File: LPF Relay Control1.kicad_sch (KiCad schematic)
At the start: 24 parts, among them K10 EA2-5NU, K3 EA2-5NU, K4 EA2-5NU, K5 EA2-5NU, K6 EA2-5NU, K7 EA2-5NU, K8 EA2-5NU, K9 EA2-5NU, Q1 BSS123, Q3 BSS123, Q4 BSS123, Q6 BSS123

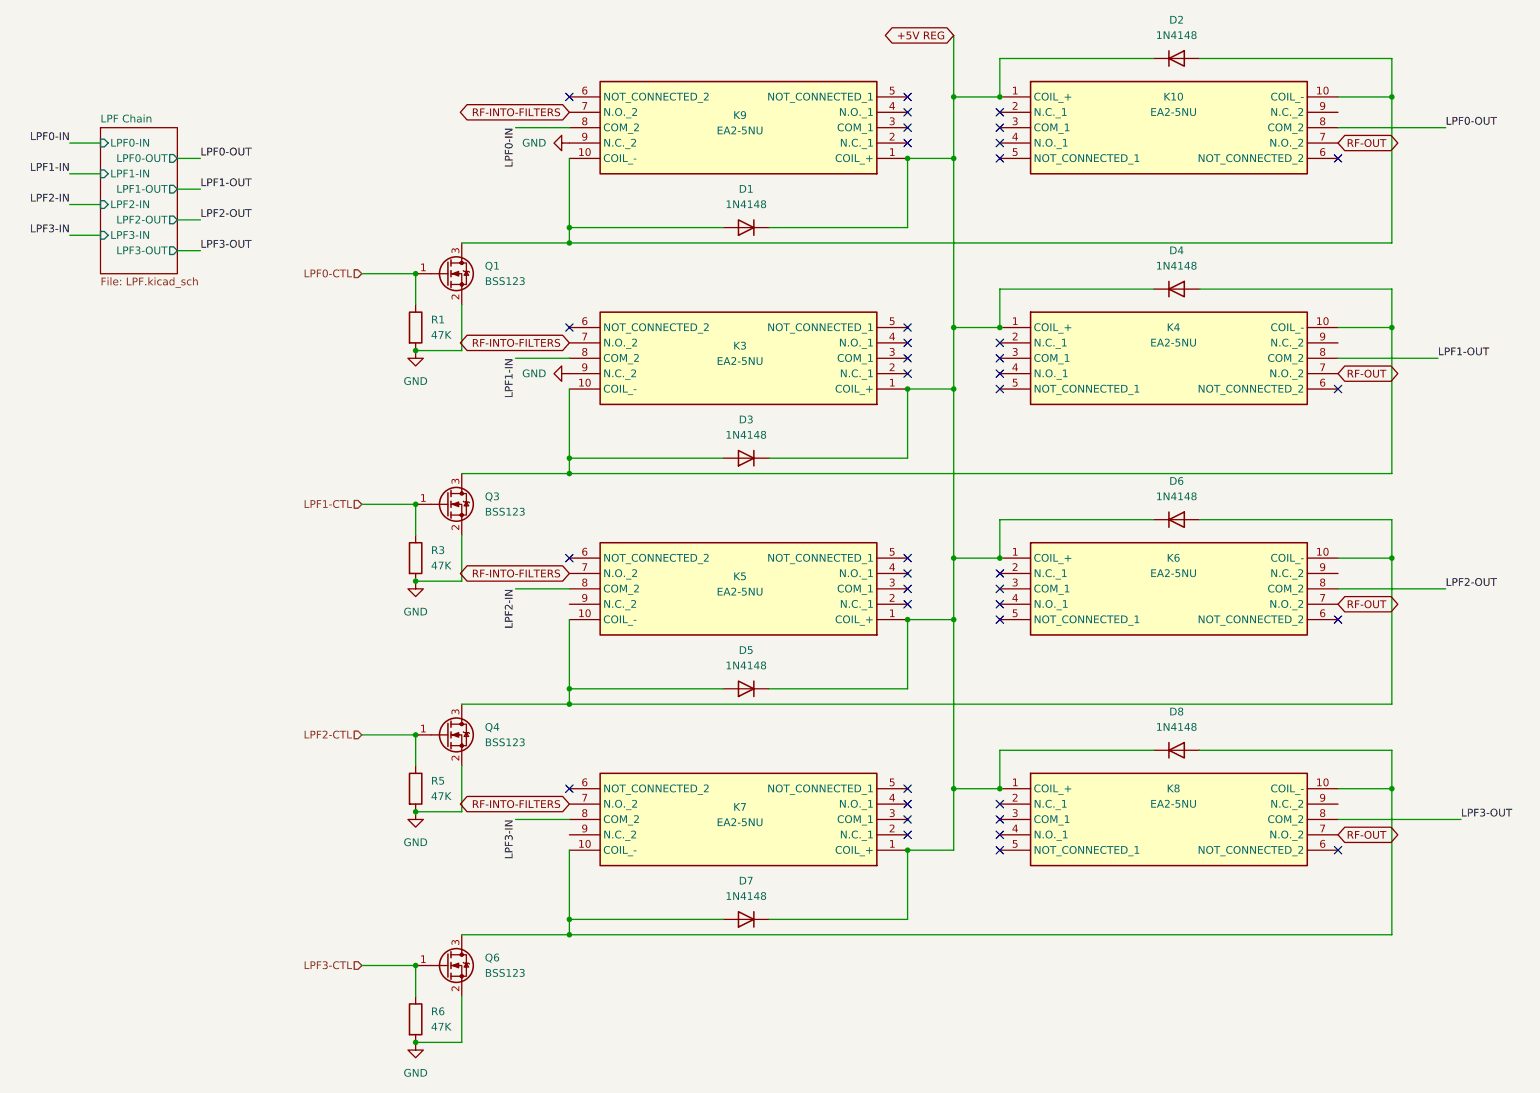
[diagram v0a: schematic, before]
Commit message: v0.6 ERC passes.  I went over it with a fine tooth comb and corrected lots of little stuff.  Ron should review all the components I have to create very carefully.  In particular, MPS-751 symbol does not look correct.
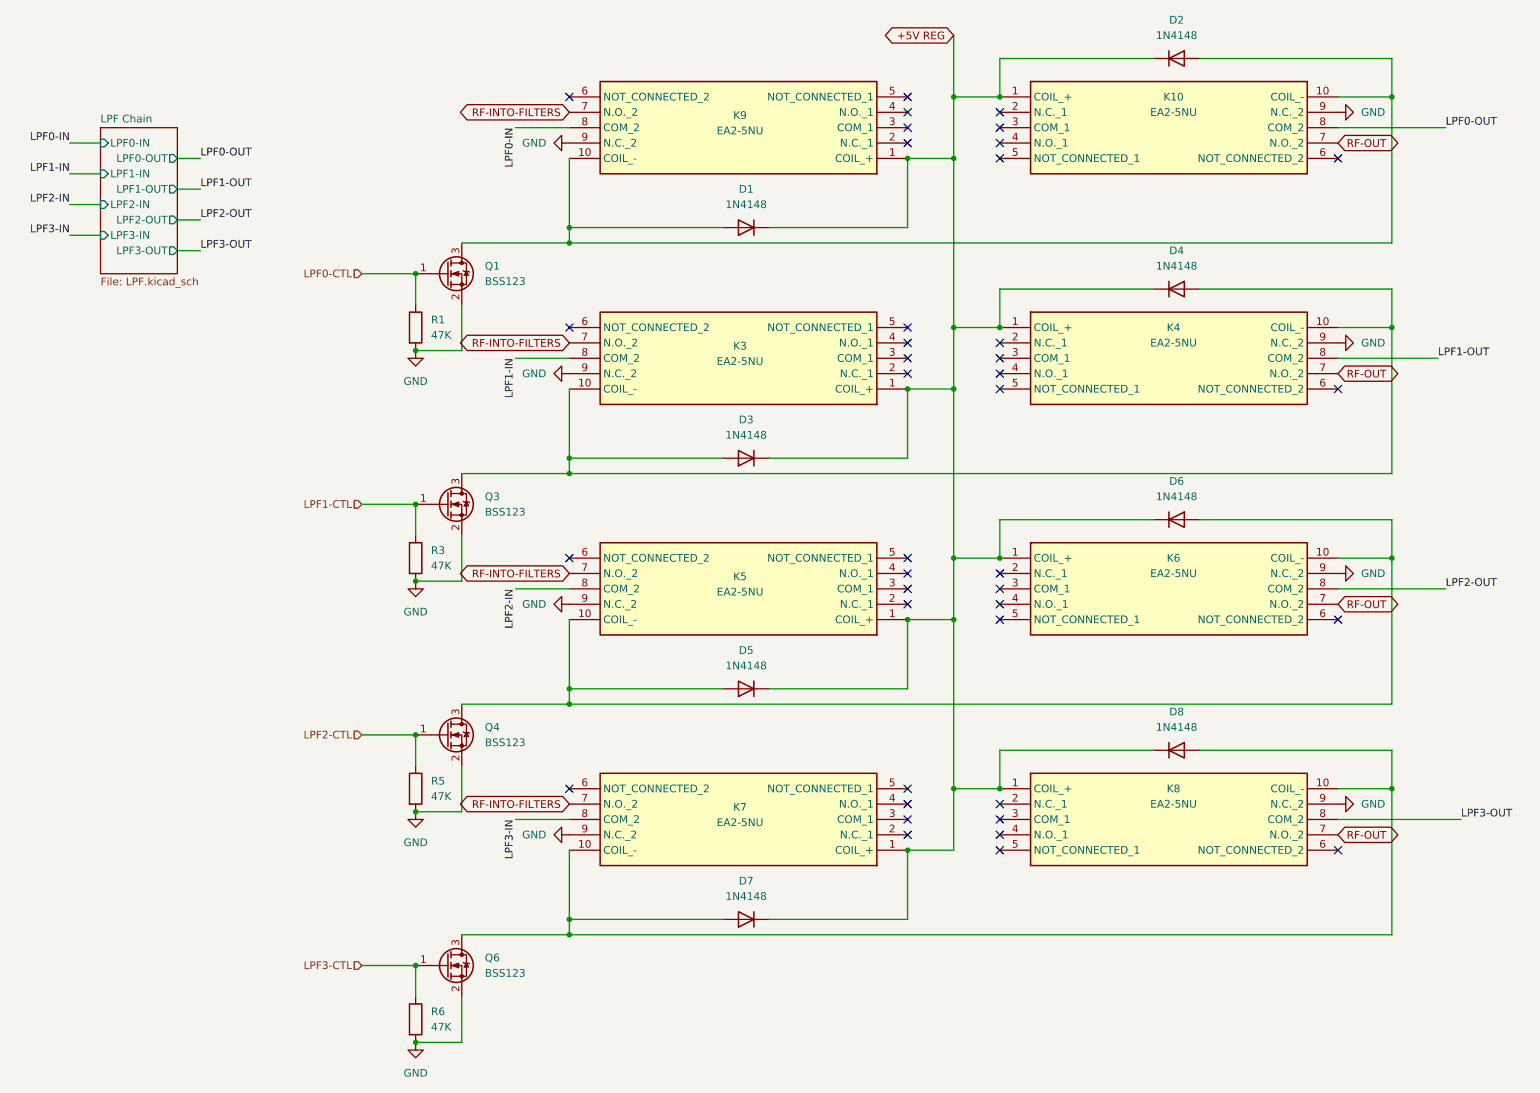
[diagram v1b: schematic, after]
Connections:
- net GND: now also K10.9 (N.C._2), K4.9 (N.C._2), K5.9 (N.C._2), K6.9 (N.C._2), K7.9 (N.C._2), K8.9 (N.C._2)
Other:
- title: QMX Amp -> QMX+ Amp

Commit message: ron came by and gave lots of feedback.  many notes on schematic for additional changes
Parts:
- R1, R3, R5, R6: footprint (none) -> Resistor_THT:R_Axial_DIN0309_L9.0mm_D3.2mm_P12.70mm_Horizontal
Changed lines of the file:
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@@
 			)
 		)
-		(property "Footprint" ""
+		(property "Footprint" "Resistor_THT:R_Axial_DIN0309_L9.0mm_D3.2mm_P12.70mm_Horizontal"
 			(at 79.502 105.41 90)
 			(effects
@@
 			)
 		)
-		(property "Footprint" ""
+		(property "Footprint" "Resistor_THT:R_Axial_DIN0309_L9.0mm_D3.2mm_P12.70mm_Horizontal"
 			(at 79.502 67.31 90)
 			(effects
@@
 			)
 		)
-		(property "Footprint" ""
+		(property "Footprint" "Resistor_THT:R_Axial_DIN0309_L9.0mm_D3.2mm_P12.70mm_Horizontal"
 			(at 79.502 143.51 90)
 			(effects
@@
 			)
 		)
-		(property "Footprint" ""
+		(property "Footprint" "Resistor_THT:R_Axial_DIN0309_L9.0mm_D3.2mm_P12.70mm_Horizontal"
 			(at 79.502 181.61 90)
 			(effects

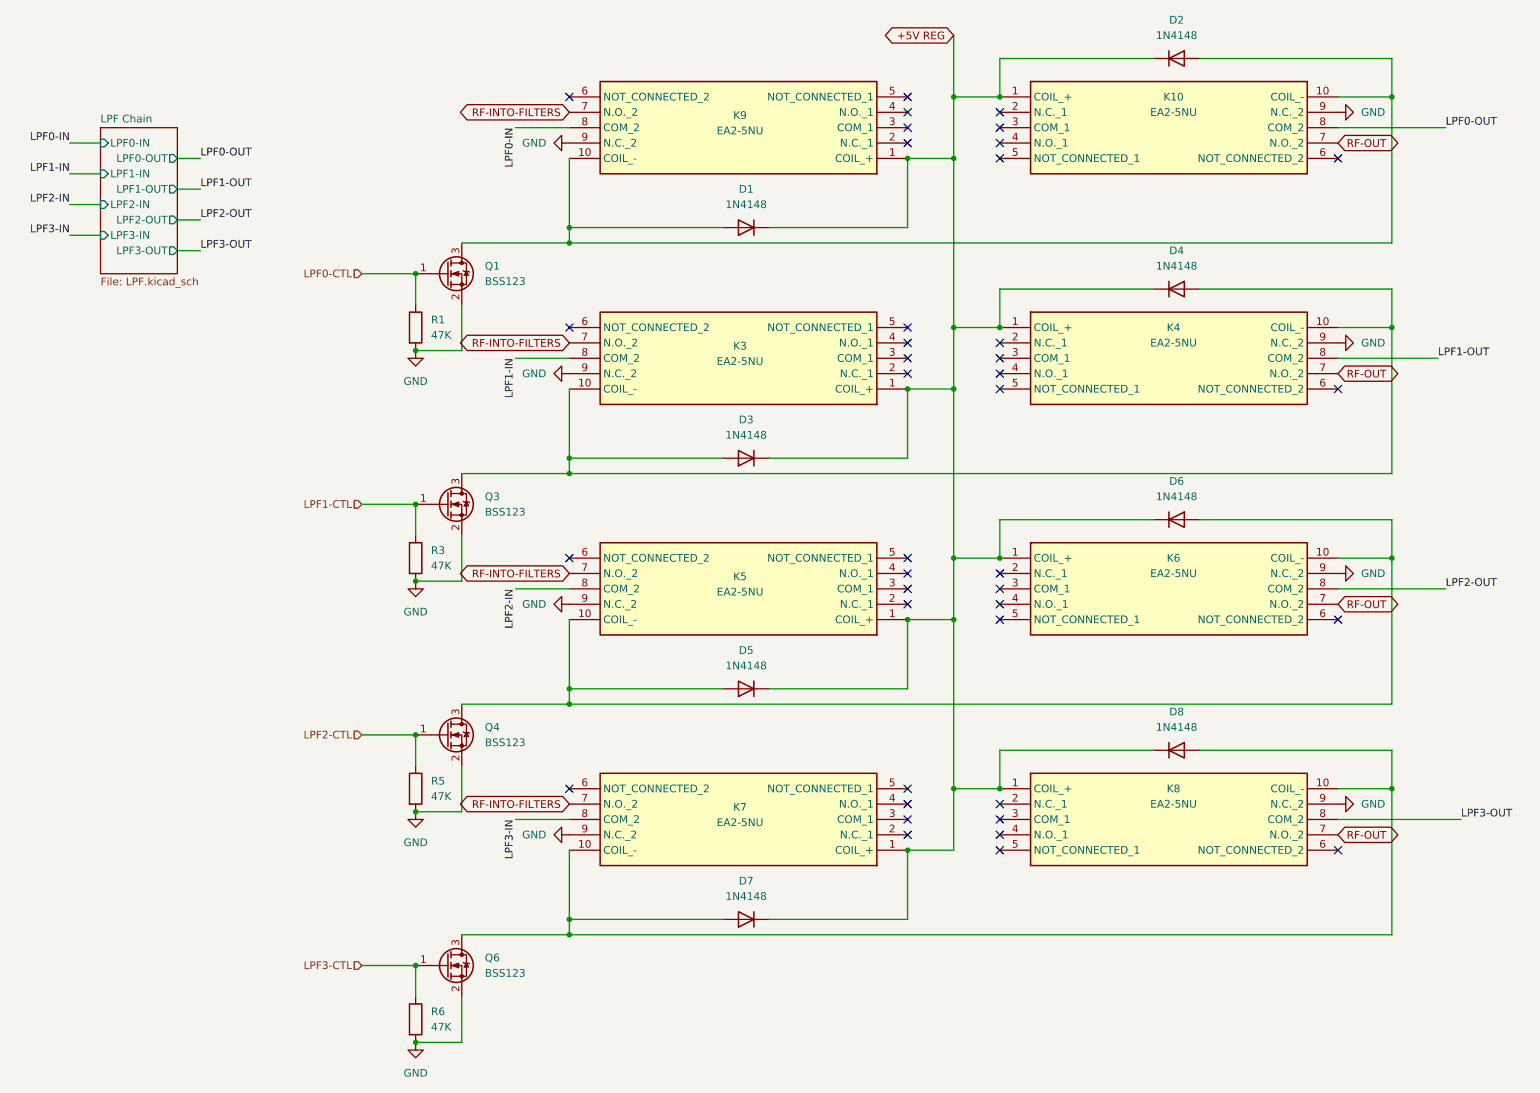
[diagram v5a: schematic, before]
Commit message: expended to all 6 LPFs.  ERC pass.  Need to check component values on new LPF page
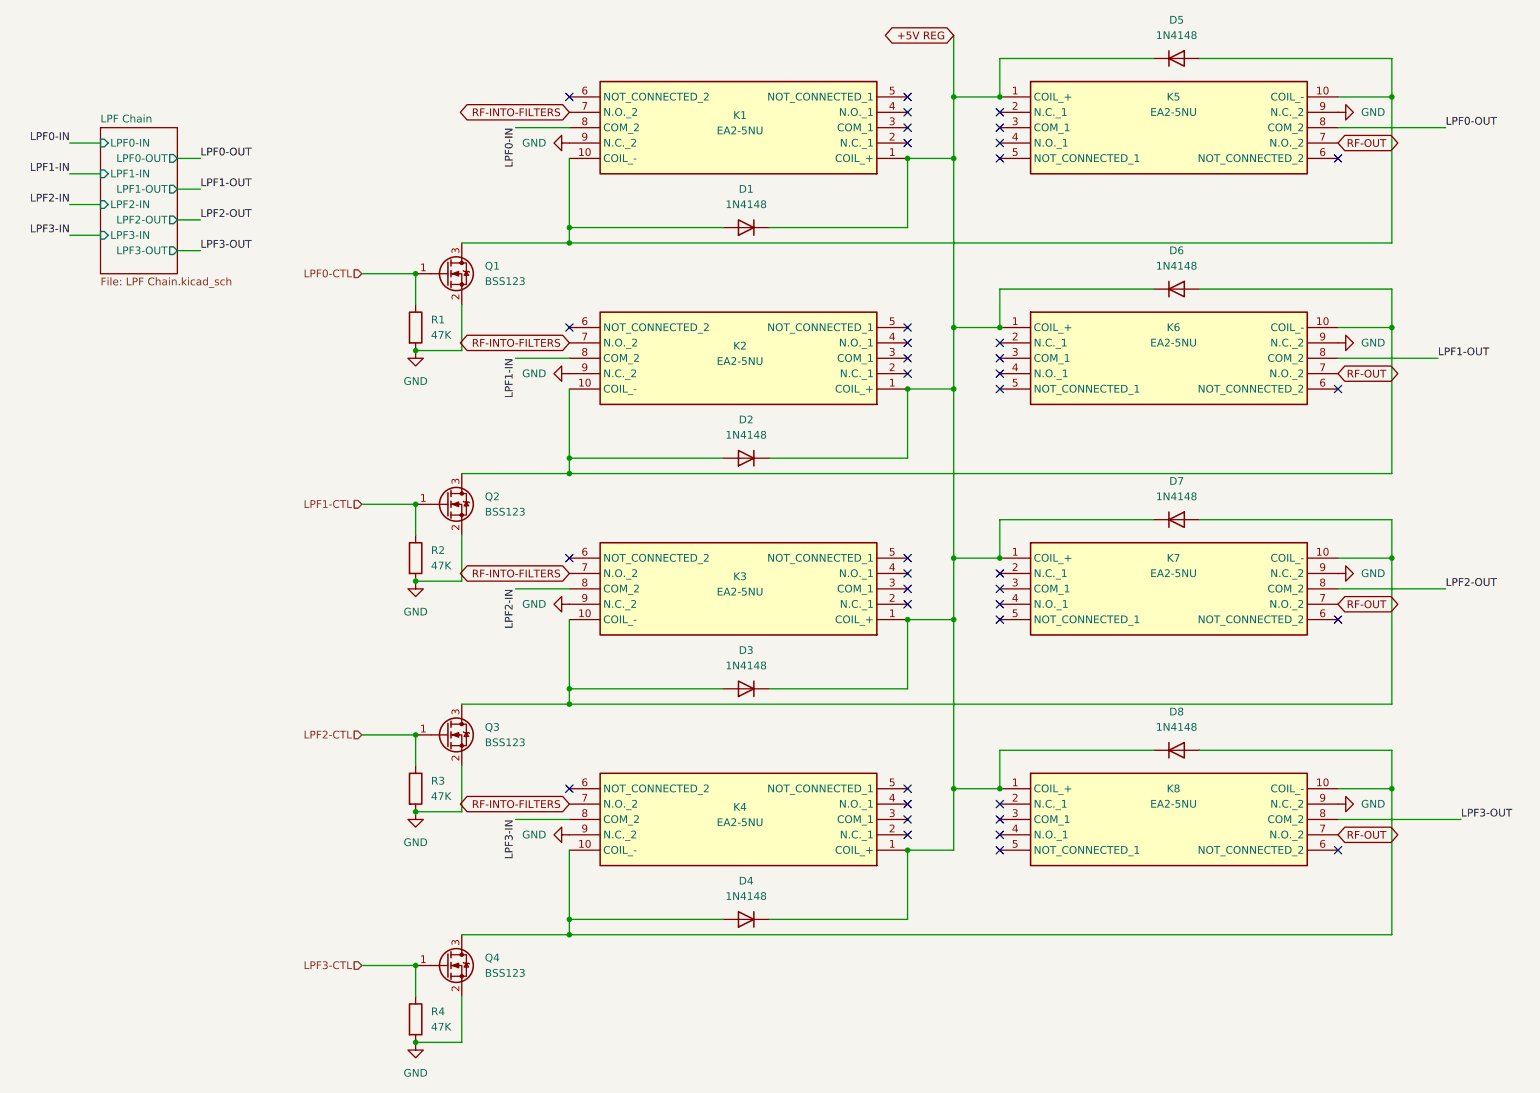
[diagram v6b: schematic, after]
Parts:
- renumbered D3 to D2, D5 to D3, D7 to D4, D2 to D5, D4 to D6, D6 to D7, K9 to K1, K3 to K2, K5 to K3, K7 to K4, K10 to K5, K4 to K6, K6 to K7, Q3 to Q2, Q4 to Q3, Q6 to Q4, R3 to R2, R5 to R3, R6 to R4
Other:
- sheet LPF Chain: file LPF.kicad_sch -> LPF Chain.kicad_sch
